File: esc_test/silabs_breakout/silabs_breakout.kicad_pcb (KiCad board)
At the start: 2 copper layers, 16.8 x 26.9 mm, 4 parts, among them IC1 C8051F330/1, P1 CONN_01X10, P2 CONN_01X10

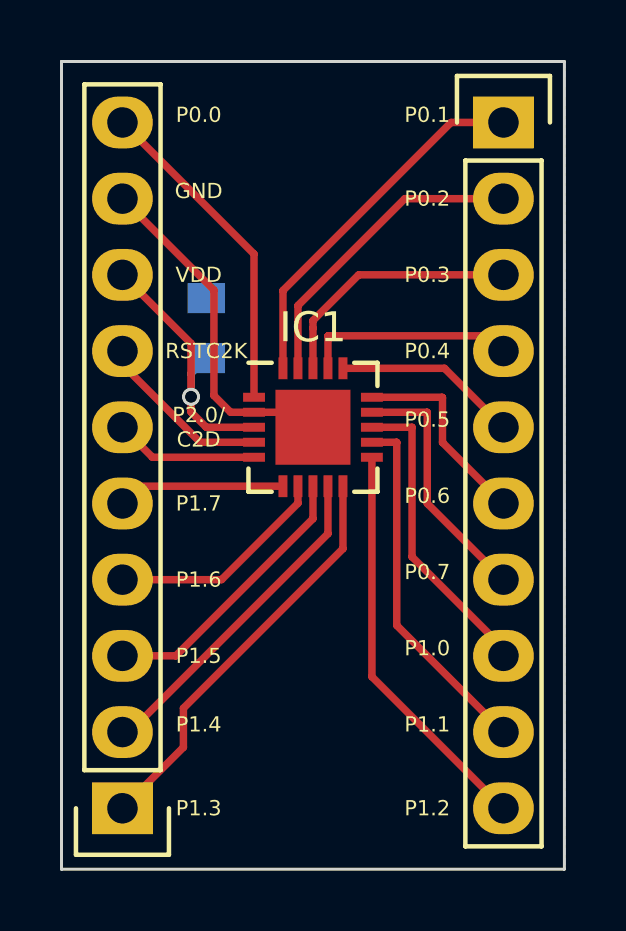
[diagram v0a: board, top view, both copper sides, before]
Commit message: Final test breakout boards sent to Oshpark.
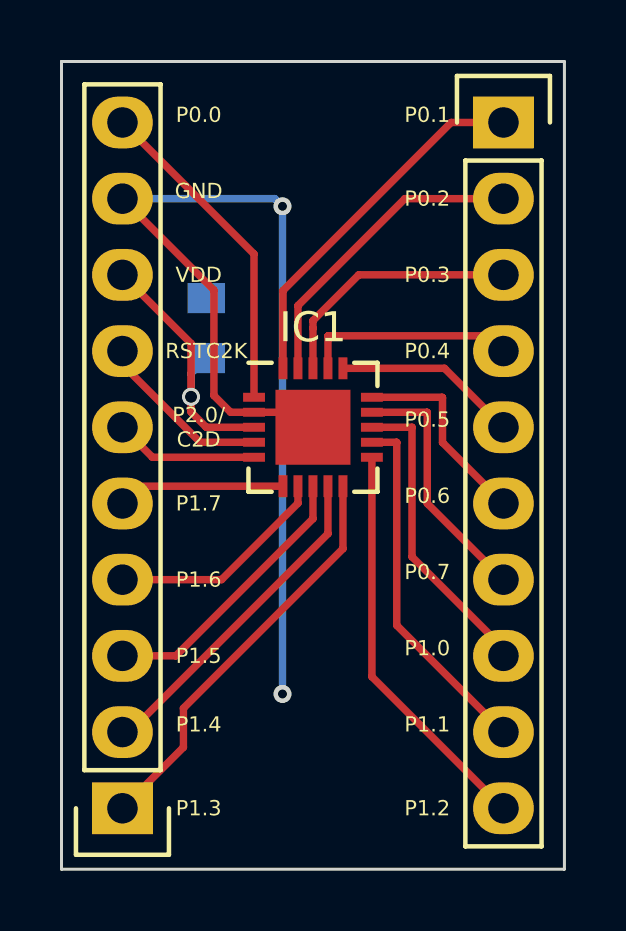
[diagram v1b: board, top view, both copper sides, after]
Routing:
- net GND: track 10.8 -> 32.5 mm, vias 0 -> 2
